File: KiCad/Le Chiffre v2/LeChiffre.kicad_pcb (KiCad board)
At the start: 2 copper layers, 228.4 x 95.7 mm, 133 parts, among them J1 Conn_01x06_Socket, J2 Conn_01x04_Female, SW1 SW_Push, SW10 SW_Push, SW11 SW_Push, SW12 SW_Push, SW13 SW_Push, SW14 SW_Push, SW15 SW_Push, SW16 SW_Push, SW17 SW_Push, SW18 SW_Push, SW19 SW_Push, SW2 SW_Push, SW20 SW_Push, SW21 SW_Push, SW22 SW_Push, SW23 SW_Push, SW24 SW_Push, SW25 SW_Push, SW26 SW_Push, SW27 SW_Push, SW28 SW_Push, SW29 SW_Push, SW3 SW_Push, SW30 SW_Push, SW31 SW_Push, SW32 SW_Push, SW33 SW_Push, SW34 SW_Push, SW35 SW_Push, SW36 Rotary_Encoder_Switch, SW37 SW_Push, SW38 SW_Push, SW39 SW_Push, SW4 SW_Push, SW5 SW_Push, SW6 SW_Push, SW7 SW_Push, SW8 SW_Push, SW9 SW_Push, U1 pro-micro-controller, U2 SN74HC595

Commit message: led data no longer bridged by default, and fixed silk for vikification message
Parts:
- JP2: value Jumper_3_Bridged12 -> Jumper_3_Open; footprint Jumper:SolderJumper-3_P1.3mm_Bridged12_RoundedPad1.0x1.5mm -> Jumper:SolderJumper-3_P1.3mm_Open_RoundedPad1.0x1.5mm
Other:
- board text added: "4) VIKified by Sadek Baroudi 2024"
- board text added: "LED data in ->"
- board text removed: "3) VIKified by Sadek Baroudi 2024"
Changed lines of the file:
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@@
     )
   )
-  (footprint "Jumper:SolderJumper-3_P1.3mm_Bridged12_RoundedPad1.0x1.5mm" (layer "B.Cu")
+  (footprint "Jumper:SolderJumper-3_P1.3mm_Open_RoundedPad1.0x1.5mm" (layer "B.Cu")
     (at 122.56 64.1875)
-    (descr "SMD Solder 3-pad Jumper, 1x1.5mm rounded Pads, 0.3mm gap, pads 1-2 bridged with 1 copper strip")
-    (tags "net tie solder jumper bridged")
-    (property "Sheetfile" "LeChiffre.kicad_sch")
-    (property "Sheetname" "")
-    (property "ki_description" "Jumper, 3-pole, pins 1+2 closed/bridged")
-    (property "ki_keywords" "Jumper SPDT")
+    (descr "SMD Solder 3-pad Jumper, 1x1.5mm rounded Pads, 0.3mm gap, open")
+    (tags "solder jumper open")
+    (property "Sheetfile" "LeChiffre.kicad_sch")
+    (property "Sheetname" "")
+    (property "ki_description" "Solder Jumper, 3-pole, open")
+    (property "ki_keywords" "Solder Jumper SPDT")
     (attr exclude_from_pos_files)
-    (net_tie_pad_groups "1, 2, 3")
-    (fp_text reference "JP2" (at 0 1.8) (layer "B.SilkS")
-        (effects (font (size 1 1) (thickness 0.15)) (justify mirror))
-    )
-    (fp_text value "Jumper_3_Bridged12" (at 0 -1.9) (layer "B.Fab")
-        (effects (font (size 1 1) (thickness 0.15)) (justify mirror))
-    )
-    (fp_poly
-      (pts
-        (xy -0.9 0.3)
-        (xy -0.4 0.3)
-        (xy -0.4 -0.3)
-        (xy -0.9 -0.3)
-      )
-      (stroke (width 0) (type solid)) (fill solid) (layer "B.Cu"))
+    (fp_text reference "JP2" (at 0.02 1.9925 180) (layer "B.SilkS") hide
+        (effects (font (size 1 1) (thickness 0.15)) (justify mirror))
+    )
+    (fp_text value "Jumper_3_Open" (at 0 -1.9 180) (layer "B.Fab")
+        (effects (font (size 1 1) (thickness 0.15)) (justify mirror))
+    )
     (fp_line (start -2.05 -0.3) (end -2.05 0.3)
       (stroke (width 0.12) (type solid)) (layer "B.SilkS"))
@@
     (effects (font (size 1.5 1.5) (thickness 0.3)) (justify mirror))
   )
+  (gr_text "LED data in ->" (at 123.04 50.74 90) (layer "B.SilkS")
+    (effects (font (size 1 1) (thickness 0.15)) (justify left bottom mirror))
+  )
   (gr_text "LED PWR" (at 152.781 54.102) (layer "B.SilkS")
     (effects (font (size 1 1) (thickness 0.15)) (justify mirror))
@@
     (effects (font (size 1 1) (thickness 0.15)) (justify mirror))
   )
-  (gr_text "3) VIKified by Sadek Baroudi 2024" (at 95.33 119.94 353) (layer "B.SilkS")
+  (gr_text "4) VIKified by Sadek Baroudi 2024" (at 95.33 119.94 353) (layer "B.SilkS")
     (effects (font (size 1.5 1.5) (thickness 0.3)) (justify mirror))
   )

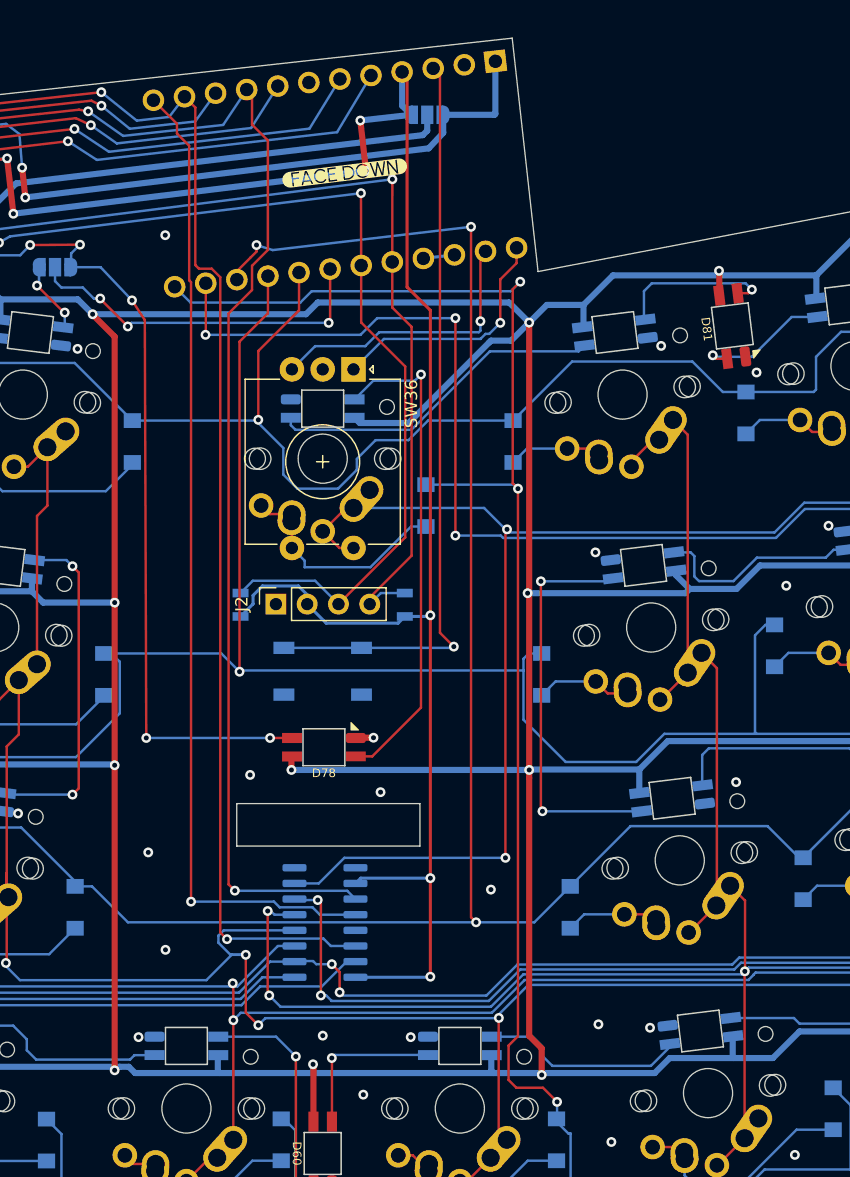
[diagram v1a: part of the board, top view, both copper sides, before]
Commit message: added better VIK cable openings
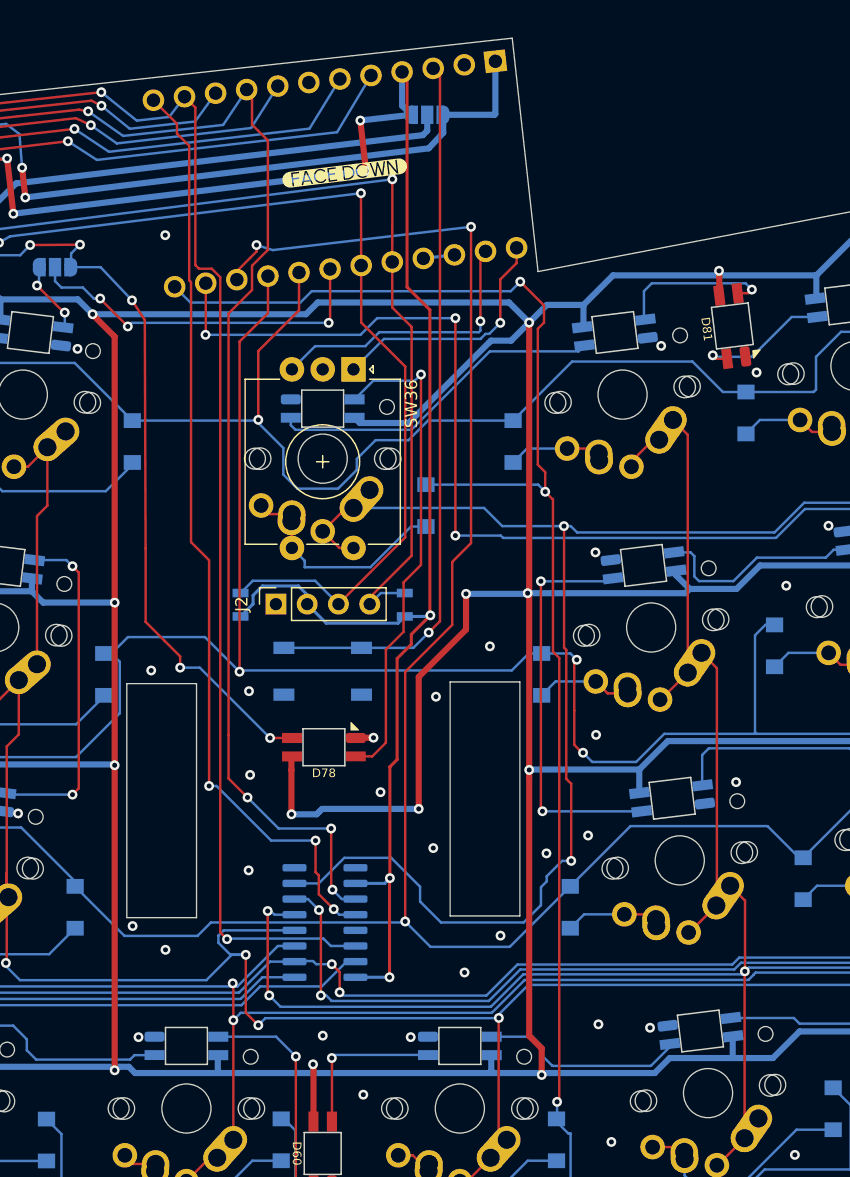
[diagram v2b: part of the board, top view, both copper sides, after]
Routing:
- net LED_PWR_OUT: track 1020.9 -> 1039.8 mm, vias 18 -> 20
- net col7: track 230.1 -> 242.2 mm
- net VCC: track 181.2 -> 176.0 mm
- net VIK_RGB_DATA: track 78.3 -> 73.4 mm
- net row2: track 247.5 -> 252.1 mm
- net SR_CS: track 80.1 -> 76.2 mm, vias 1 -> 3
- net RST: track 61.5 -> 58.7 mm
- net SCLK: track 122.0 -> 119.9 mm, vias 3 -> 5
- net row1: track 250.2 -> 251.8 mm, vias 1 -> 3
- net GND: vias 82 -> 92
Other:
- outline, holes or cut-outs redrawn

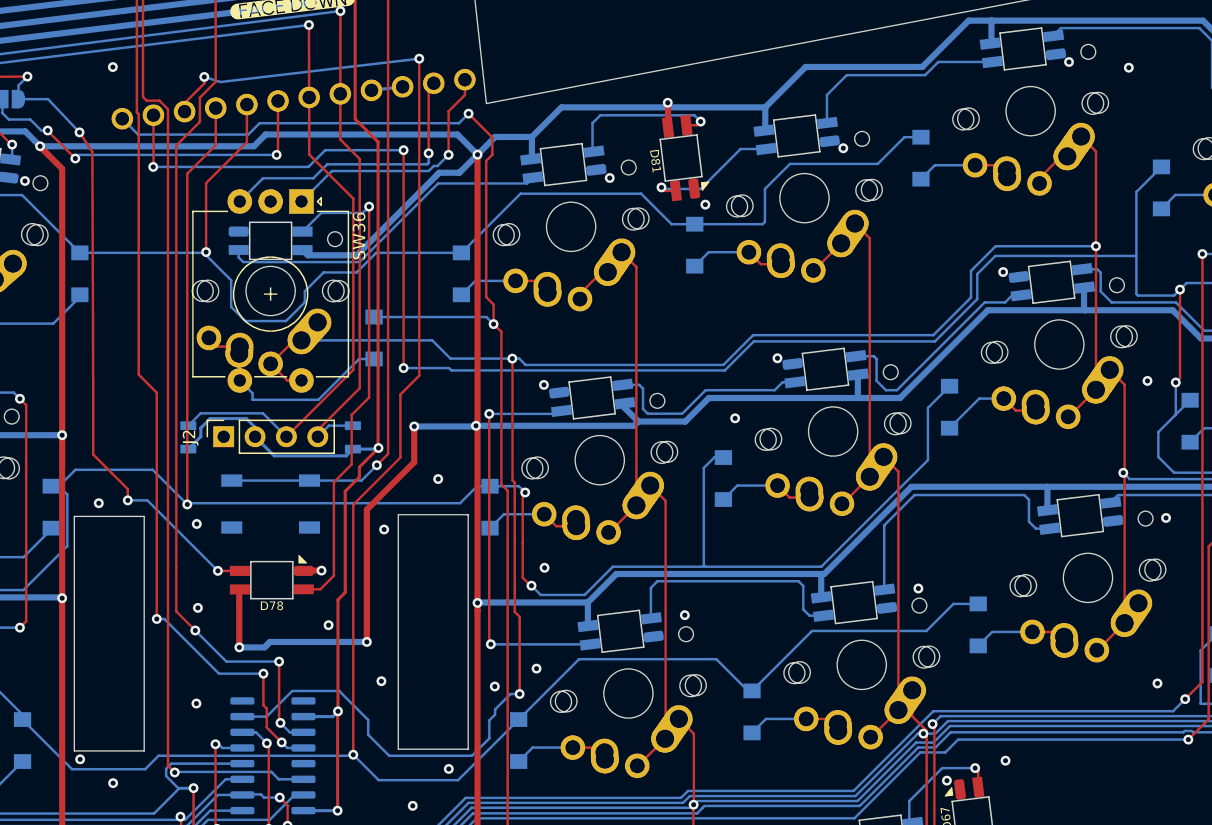
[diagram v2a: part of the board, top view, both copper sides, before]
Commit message: added trackpoint mounting support
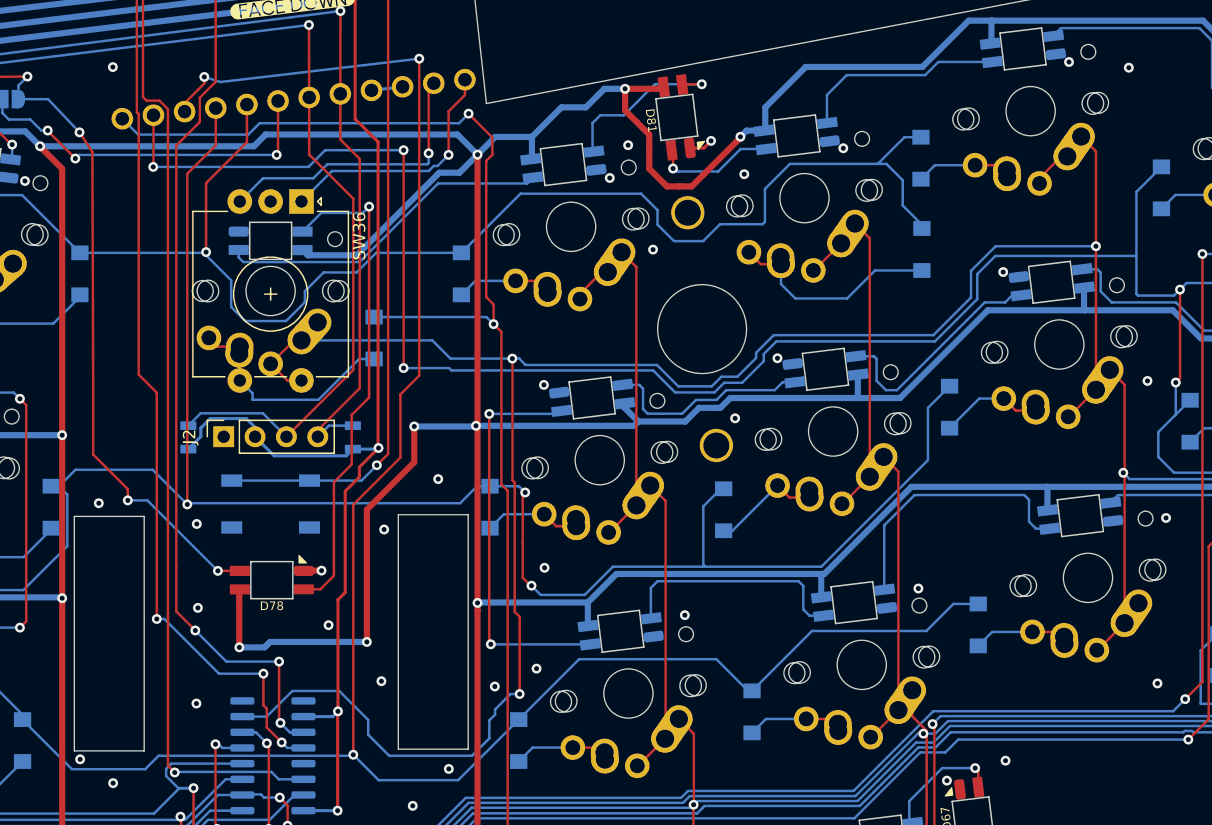
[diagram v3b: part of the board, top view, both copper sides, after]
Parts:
- added H1: MountingHole, dek:TPSensorModule, F.Cu at (179.3, 82.8)
- moved D22 18.4 mm to (197.1, 76.4)
- moved D81 3.31 mm to (177.2, 65.7)
- moved D23 2.53 mm to (181.0, 97.5)
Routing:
- net Net-(D22-K): track 7.86 -> 17.4 mm
- net LED_PWR_OUT: track 1039.8 -> 1049.3 mm, vias 20 -> 21
- net row0: track 193.8 -> 202.8 mm
- net row1: track 251.8 -> 249.0 mm
- net GND: track 9.71 -> 11.7 mm, vias 92 -> 95
- net row3: track 249.0 -> 250.8 mm
- net col7: track 242.2 -> 243.9 mm
- net Net-(D80-DIN): track 12.7 -> 13.9 mm
- net Net-(D81-DIN): track 11.2 -> 9.93 mm
- net Net-(D23-K): track 7.86 -> 8.89 mm
